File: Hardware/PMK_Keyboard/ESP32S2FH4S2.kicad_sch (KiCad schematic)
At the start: 32 parts, among them J401 Conn_01x08_Female, U401 ESP32-S2FH4, Y401 40MHz

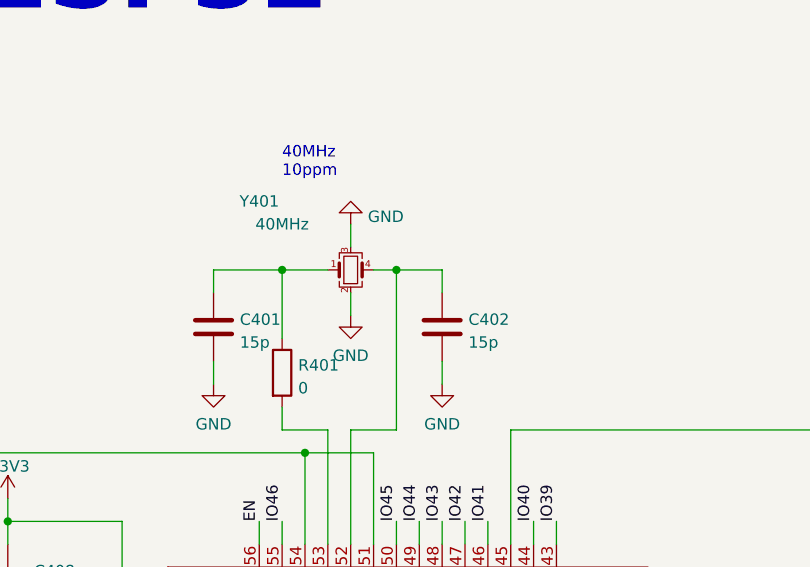
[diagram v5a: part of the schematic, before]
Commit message: Added the correct ref for USB C connector
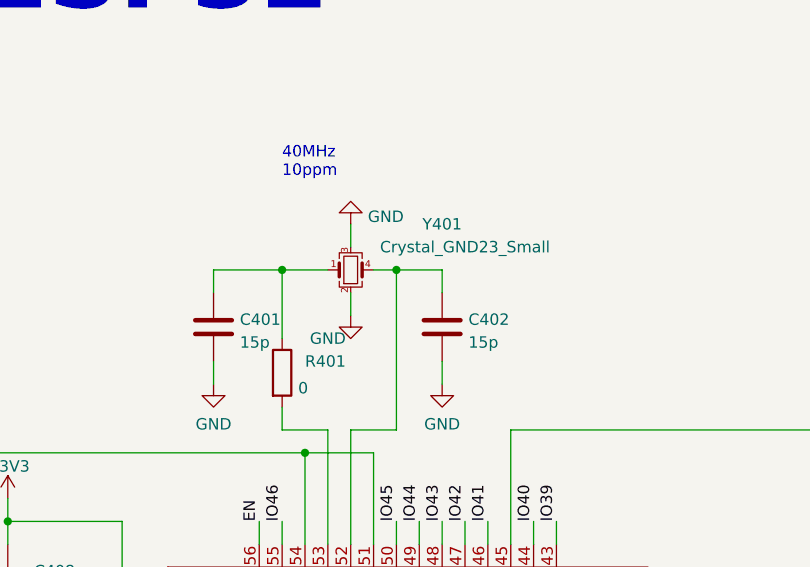
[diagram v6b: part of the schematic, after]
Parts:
- removed Y401: 40MHz, Component_lib:Crystal_SMD_2016-4Pin_2.0x1.6mm, symbol Device:Crystal_GND23_Small
- added Y401: Crystal_GND23_Small, Component_lib:Crystal_SMD_2016-4Pin_2.0x1.6mm, symbol Component_lib:Crystal_GND23_Small
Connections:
- net GND: now also Y401.2, Y401.3
- net at C401.1, R401.1: now also Y401.1
- net at C402.1, U401.52 (XTAL_N): now also Y401.4
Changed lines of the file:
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@@
   )
   (symbol (lib_id "power:GND") (at 91.44 68.58 0) (unit 1)
-    (in_bom yes) (on_board yes) (fields_autoplaced)
+    (in_bom yes) (on_board yes)
     (property "Reference" "#PWR0404" (id 0) (at 91.44 74.93 0)
       (effects (font (size 1.27 1.27)) hide)
     )
-    (property "Value" "GND" (id 1) (at 91.44 73.0234 0))
+    (property "Value" "GND" (id 1) (at 88.9 71.12 0))
     (property "Footprint" "" (id 2) (at 91.44 68.58 0)
       (effects (font (size 1.27 1.27)) hide)
@@
     )
     (pin "1")
+  )
+  (symbol (lib_id "Component_lib:Crystal_GND23_Small") (at 91.44 63.5 0) (unit 1)
+    (in_bom yes) (on_board yes)
+    (property "Reference" "Y401" (id 0) (at 101.6 58.42 0))
+    (property "Value" "Crystal_GND23_Small" (id 1) (at 104.14 60.96 0))
+    (property "Footprint" "Component_lib:Crystal_SMD_2016-4Pin_2.0x1.6mm" (id 2) (at 91.44 63.5 0)
+      (effects (font (size 1.27 1.27)) hide)
+    )
+    (property "Datasheet" "https://www.mouser.ch/ProductDetail/ECS/ECS-400-10-37B-CKY-TR3?qs=TCDPyi3sCW2VtaBG%252B2IQWA%3D%3D" (id 3) (at 91.44 63.5 0)
+      (effects (font (size 1.27 1.27)) hide)
+    )
+    (pin "1")
+    (pin "2")
+    (pin "3")
+    (pin "4")
   )
   (symbol (lib_id "power:GND") (at 144.78 149.86 0) (unit 1)
@@
     (pin "1")
   )
-  (symbol (lib_id "Device:Crystal_GND23_Small") (at 91.44 63.5 0) (unit 1)
-    (in_bom yes) (on_board yes)
-    (property "Reference" "Y401" (id 0) (at 81.28 55.88 0))
-    (property "Value" "40MHz" (id 1) (at 83.82 58.42 0))
-    (property "Footprint" "Component_lib:Crystal_SMD_2016-4Pin_2.0x1.6mm" (id 2) (at 91.44 63.5 0)
-      (effects (font (size 1.27 1.27)) hide)
-    )
-    (property "Datasheet" "~" (id 3) (at 91.44 63.5 0)
-      (effects (font (size 1.27 1.27)) hide)
-    )
-    (pin "1")
-    (pin "2")
-    (pin "3")
-    (pin "4")
-  )
   (symbol (lib_id "power:GND") (at 157.48 149.86 0) (unit 1)
     (in_bom yes) (on_board yes) (fields_autoplaced)
@@
   )
   (symbol (lib_id "Component lib:R") (at 83.82 71.12 0) (unit 1)
-    (in_bom yes) (on_board yes) (fields_autoplaced)
-    (property "Reference" "R401" (id 0) (at 85.598 74.0953 0)
-      (effects (font (size 1.27 1.27)) (justify left))
-    )
+    (in_bom yes) (on_board yes)
+    (property "Reference" "R401" (id 0) (at 86.36 73.66 0)
+      (effects (font (size 1.27 1.27)) (justify left))
+    )

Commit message: Routing is almost done
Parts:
- removed Y401: Crystal_GND23_Small, Component_lib:Crystal_SMD_2016-4Pin_2.0x1.6mm, symbol Component_lib:Crystal_GND23_Small
- added J402: Conn_01x03_Socket, Connector_PinHeader_2.54mm:PinHeader_1x03_P2.54mm_Vertical, symbol Connector:Conn_01x03_Socket
- added Y601: Crystal_GND24_Small, Component_lib:Crystal_SMD_2016-4Pin_2.0x1.6mm, symbol Device:Crystal_GND24_Small
- D401: footprint LED_SMD:LED_0402_1005Metric -> Component_lib:LED_0402_1005Metric_DUALSIDE
- J401: footprint Connector_PinHeader_1.00mm:PinHeader_1x08_P1.00mm_Vertical -> Connector_PinHeader_1.27mm:PinHeader_1x08_P1.27mm_Vertical
- R402: footprint Resistor_SMD:R_0201_0603Metric -> Resistor_SMD:R_0402_1005Metric
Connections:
- net IO14 is gone; now on net BTN: U401.19 (GPIO14)
- net IO21 is gone; now on net LED_EN: U401.28 (GPIO21)
- net IO39 is gone; now on net LED_MOSI: U401.43 (MTCK)
- net BTN: no longer U401.14 (GPIO9)
- net DOWN: now also U401.16 (GPIO11); no longer U401.11 (GPIO6)
- net GND: now also J402.3 (Pin_3), Y601.2, Y601.4
- net LED: now also U401.14 (GPIO9); no longer U401.9 (GPIO4)
- net LED_EN: no longer U401.22 (XTAL_32K_N)
- net LED_MOSI: no longer R402.1, U401.21 (XTAL_32K_P)
- net LEFT: now also U401.17 (GPIO12); no longer U401.12 (GPIO7)
- net PL: now also U401.12 (GPIO7); no longer U401.18 (GPIO13)
- net RIGHT: now also U401.18 (GPIO13); no longer U401.13 (GPIO8)
- net SR_CLK: now also U401.11 (GPIO6); no longer U401.16 (GPIO11)
- net SR_CS: now also U401.10 (GPIO5); no longer U401.17 (GPIO12)
- net SR_MISO: now also U401.13 (GPIO8); no longer U401.15 (GPIO10)
- net UP: now also U401.15 (GPIO10); no longer U401.10 (GPIO5)
- net at C401.1, R401.1: now also Y601.1
- net at C402.1, U401.52 (XTAL_N): now also Y601.3
- net LED_NET: now reaches D401.2 (A), R402.2
- net IO33: now reaches U401.37 (GPIO33)
- net IO34: now reaches U401.38 (GPIO34)
- net IO35: now reaches U401.39 (GPIO35)
- net IO36: now reaches U401.40 (GPIO36)
- net IO37: now reaches U401.41 (GPIO37)
- net IO38: now reaches U401.42 (GPIO38)
- net IO43 renamed TX0
- net TX0: now also J402.2 (Pin_2)
- net IO44 renamed RX0
- net RX0: now also J402.1 (Pin_1)
- new net IO15: R402.1
- new net IO16: U401.22 (XTAL_32K_N)
- new net IO4: U401.9 (GPIO4)
